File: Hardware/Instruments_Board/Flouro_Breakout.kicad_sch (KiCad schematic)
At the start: 12 parts, among them J1 RJ45_LED_Shielded, U1 Teensy4.1_DEV-16771, U2 3V3 OKI

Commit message: Running traces
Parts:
- added H1, H2, H3: MountingHole, MountingHole:MountingHole_3.2mm_M3, symbol Mechanical:MountingHole
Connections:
- net T+: now reaches J1.1, U1.T+
- net ETH_LED: now reaches J1.10, U1.LED
- net T-: now reaches J1.3, U1.T (T-)
- net R+: now reaches J1.4, U1.R+
- net R-: now reaches J1.6, U1.R (R-)
- net 365_CTRL: now reaches U1.28 (RX7)
- net 365_CTRL: now also Conn3.2
- net 310_CTRL: now reaches U1.29 (TX7)
- net 310_CTRL: now also Conn3.3
- net 280_CTRL: now reaches U1.30 (CRX3)
- net 280_CTRL: now also Conn3.4
- net 275_CTRL: now reaches U1.31 (CTX3)
- net 275_CTRL: now also Conn3.5
- net 260_CTRL: now reaches U1.32 (OUT1B)
- net 260_CTRL: now also Conn3.6
- net 260nm: no longer names the net of U1.27 (A13)
- net 260nm: no longer Conn3.6
- net 275nm: no longer names the net of U1.38 (A14)
- net 275nm: no longer Conn3.5
- net 280nm: no longer names the net of U1.39 (A15)
- net 280nm: no longer Conn3.4
- net 310nm: no longer names the net of U1.40 (A16)
- net 310nm: no longer Conn3.3
- net 365nm: no longer names the net of U1.41 (A17)
- net 365nm: no longer Conn3.2

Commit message: finished fluoro breakout
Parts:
- removed Conn3: Molex_SL_07, MRDT_Connectors:MOLEX_SL_07_Vertical, symbol MRDT_Connectors:Molex_SL_07
- added D2, D3, D4, D5, D6: Green, LED_SMD:LED_0603_1608Metric_Pad1.05x0.95mm_HandSolder, symbol Device:LED
- added H?: MountingHole, MRDT_Drill_Holes:4_40_Hole_Corner, symbol Mechanical:MountingHole
- added J2: Conn_01x06_Female, Connector_Molex:Molex_SL_171971-0006_1x06_P2.54mm_Vertical, symbol Connector:Conn_01x06_Female
- added Q1, Q2, Q5, Q7, Q9: BSS138, Package_TO_SOT_SMD:SOT-23, symbol Transistor_FET:BSS138
- added Q10, Q3, Q4, Q6, Q8: IRF7606PBF, Package_SO:SOP-8_3.9x4.9mm_P1.27mm, symbol Transistor_FET:IRF7606PBF
- added R10, R14, R18, R2, R3: 4.7k, Resistor_SMD:R_0603_1608Metric_Pad0.98x0.95mm_HandSolder, symbol Device:R
- added R11, R12, R15, R16, R19, R20, R4, R5, R6, R7: 10k, Resistor_SMD:R_0603_1608Metric_Pad0.98x0.95mm_HandSolder, symbol Device:R
- added R13, R17, R21, R8, R9: 1k, Resistor_SMD:R_0603_1608Metric_Pad0.98x0.95mm_HandSolder, symbol Device:R
- H1, H2, H3: footprint MountingHole:MountingHole_3.2mm_M3 -> MRDT_Drill_Holes:4_40_Hole_Corner
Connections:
- net +12V: now also Q10.1 (S), Q10.2 (S), Q10.3 (S), Q3.1 (S), Q3.2 (S), Q3.3 (S), Q4.1 (S), Q4.2 (S), Q4.3 (S), Q6.1 (S), Q6.2 (S), Q6.3 (S), Q8.1 (S), Q8.2 (S), Q8.3 (S), R11.1, R15.1, R19.1, R4.1, R6.1
- net 260_CTRL: now also U1.27 (A13), Q2.1 (G), R3.1
- net 275_CTRL: now also U1.38 (A14), Q9.1 (G), R18.1
- net 280_CTRL: now also U1.39 (A15), Q7.1 (G), R14.1
- net 310_CTRL: now also U1.40 (A16), Q5.1 (G), R10.1
- net 365_CTRL: now also U1.41 (A17), Q1.1 (G), R2.1
- net GND: now also D2.1 (K), D3.1 (K), D4.1 (K), D5.1 (K), D6.1 (K), J2.6 (Pin_6), Q1.2 (S), Q2.2 (S), Q5.2 (S), Q7.2 (S), Q9.2 (S), R10.2, R14.2, R18.2, R2.2, R3.2
- new net: Q4.4 (G), R6.2, R7.1
- new net: Q6.4 (G), R11.2, R12.1
- new net: D5.2 (A), R17.2
- new net: D3.2 (A), R9.2
- new net: Q9.3 (D), R20.2
- new net: Q3.4 (G), R4.2, R5.1
- new net: Q10.4 (G), R19.2, R20.1
- new net: D2.2 (A), R8.2
- new net: Q1.3 (D), R5.2
- new net: Q8.4 (G), R15.2, R16.1
- new net: Q5.3 (D), R12.2
- new net: Q2.3 (D), R7.2
- new net: D4.2 (A), R13.2
- new net: D6.2 (A), R21.2
- new net: Q7.3 (D), R16.2
- new net 260nm: J2.5 (Pin_5), Q4.5 (D), Q4.6 (D), Q4.7 (D), Q4.8 (D), R9.1
- new net 275nm: J2.4 (Pin_4), Q10.5 (D), Q10.6 (D), Q10.7 (D), Q10.8 (D), R21.1
- new net 280nm: J2.3 (Pin_3), Q8.5 (D), Q8.6 (D), Q8.7 (D), Q8.8 (D), R17.1
- new net 310nm: J2.2 (Pin_2), Q6.5 (D), Q6.6 (D), Q6.7 (D), Q6.8 (D), R13.1
- new net 365nm: J2.1 (Pin_1), Q3.5 (D), Q3.6 (D), Q3.7 (D), Q3.8 (D), R8.1
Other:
- note removed: "Teesny/Ehternet"
- note removed: "UV LED Connector"
- moved on the sheet: U1

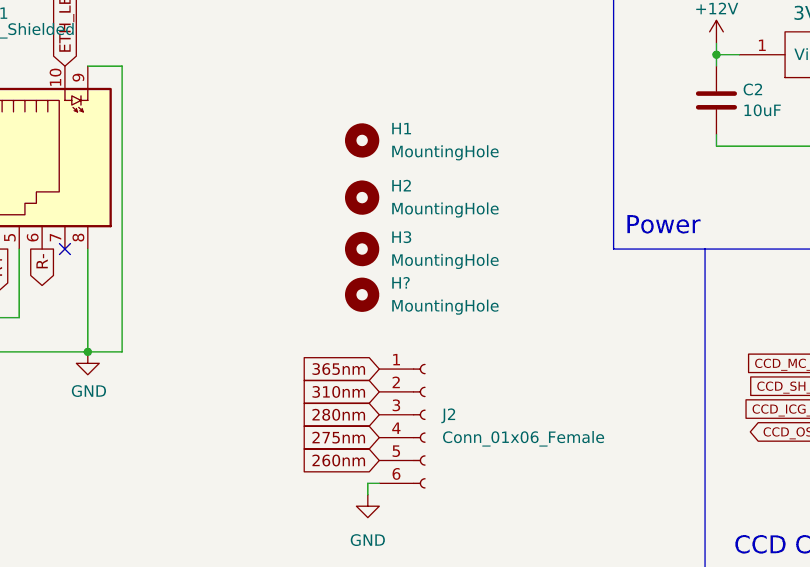
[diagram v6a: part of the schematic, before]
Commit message: updated mounting holes
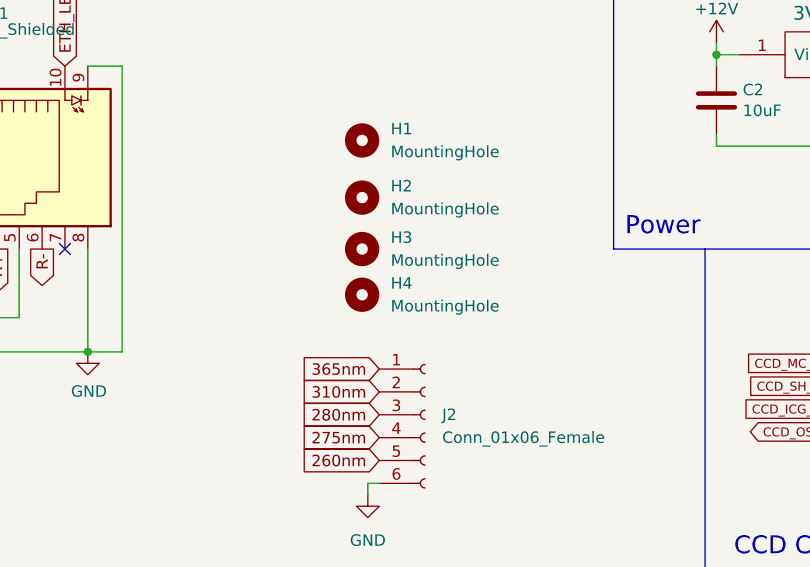
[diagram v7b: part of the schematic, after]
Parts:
- gave numbers to parts that had none: 1
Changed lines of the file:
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@@
   (symbol (lib_id "Mechanical:MountingHole") (at 154.94 52.07 0) (unit 1)
     (in_bom yes) (on_board yes) (fields_autoplaced)
-    (property "Reference" "H?" (id 0) (at 158.115 50.7999 0)
+    (property "Reference" "H4" (id 0) (at 158.115 50.7999 0)
       (effects (font (size 1.27 1.27)) (justify left))
     )
@@
     )
     (path "/ac34bb12-007f-4202-a3a5-1c322457208e"
-      (reference "H?") (unit 1) (value "MountingHole") (footprint "MRDT_Drill_Holes:4_40_Hole_Corner")
+      (reference "H4") (unit 1) (value "MountingHole") (footprint "MRDT_Drill_Holes:4_40_Hole_Corner")
     )
     (path "/269f3339-dc77-41ad-8061-e06ca80de4be"

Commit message: page edits for printing
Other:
- title: Flourometer_Breakout -> Instruments Board
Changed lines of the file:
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@@
   (paper "A4")
   (title_block
-    (title "Flourometer_Breakout")
+    (title "Instruments Board")
     (rev "1")
     (company "MRDT")
